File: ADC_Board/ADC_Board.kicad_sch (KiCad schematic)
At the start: 0 parts

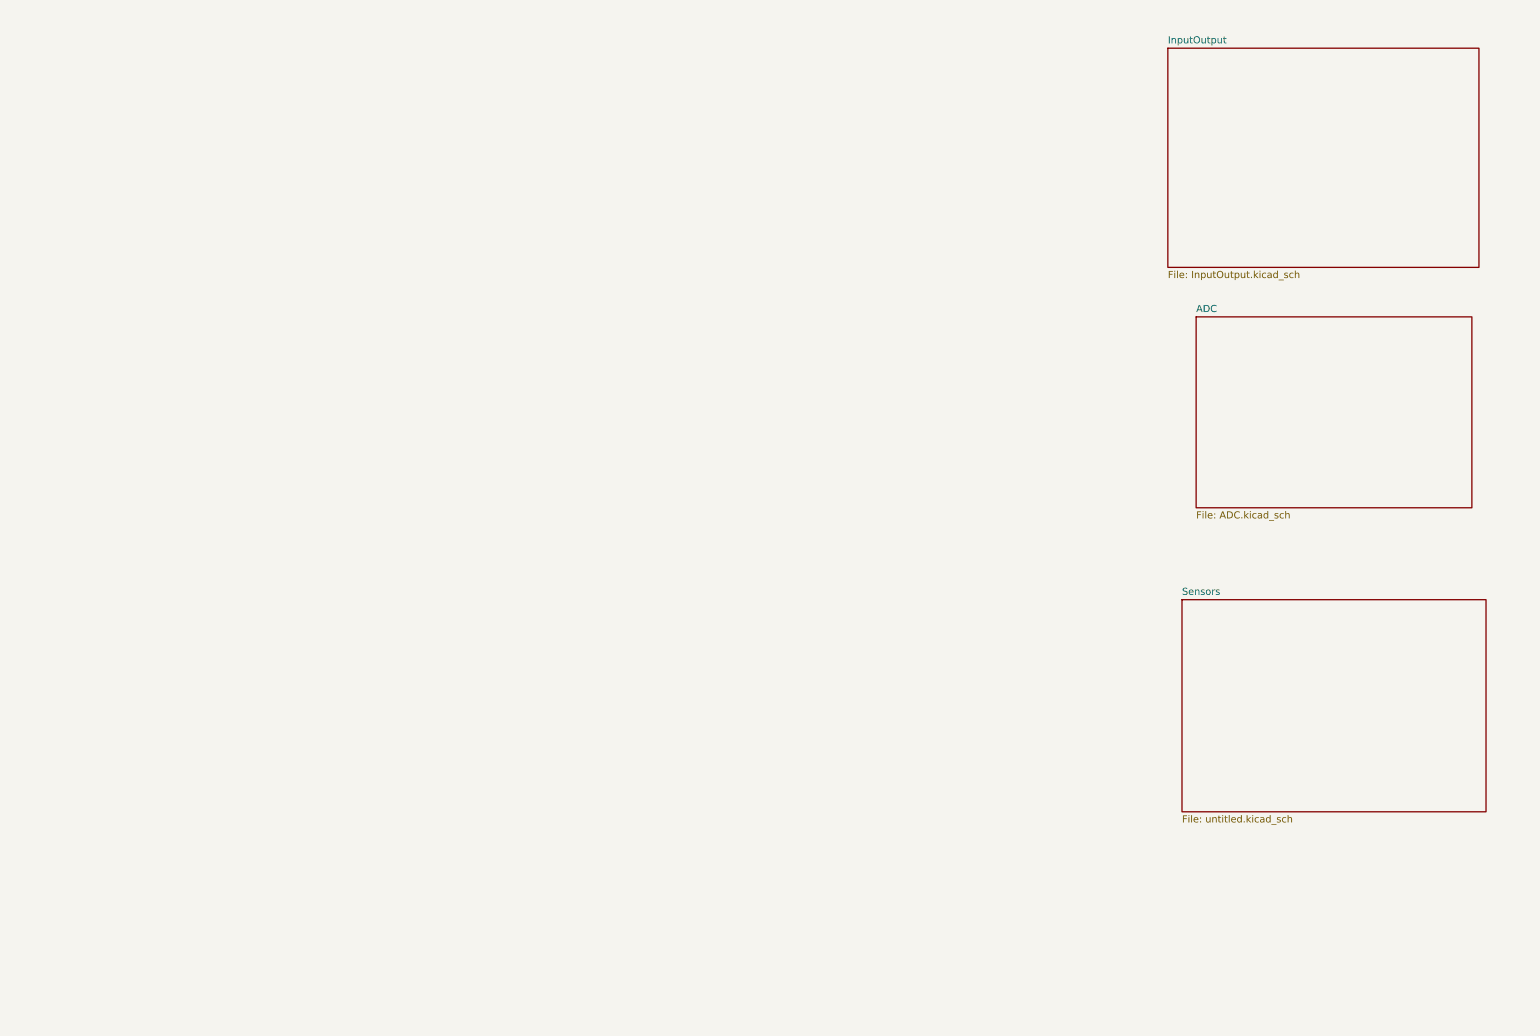
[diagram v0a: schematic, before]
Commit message: Changes made after v1 to address Lakshay and Ishaans comments
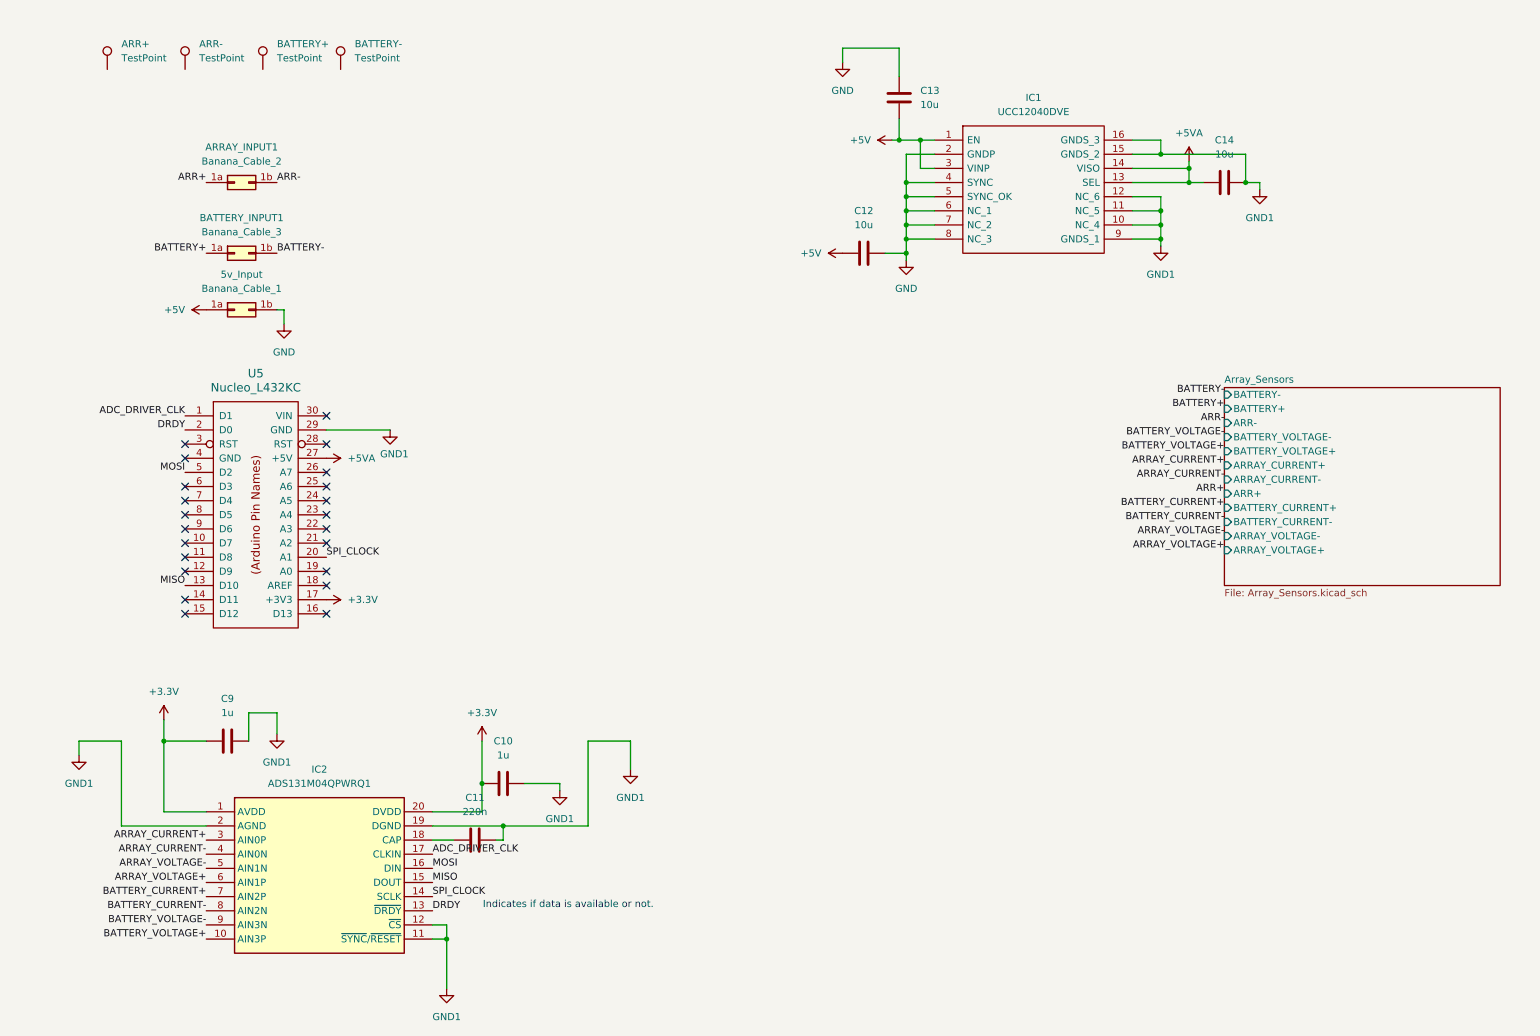
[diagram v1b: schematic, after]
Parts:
- added 5v_Input: Banana_Cable_1, symbol Connector_Generic:Conn_02x01_Row_Letter_Last
- added ARR+, ARR-, BATTERY+, BATTERY-: TestPoint, symbol Connector:TestPoint
- added ARRAY_INPUT1: Banana_Cable_2, symbol Connector_Generic:Conn_02x01_Row_Letter_Last
- added BATTERY_INPUT1: Banana_Cable_3, symbol Connector_Generic:Conn_02x01_Row_Letter_Last
- added C10, C9: 1u, symbol Device:C
- added C11: 220n, symbol Device:C
- added C12, C13, C14: 10u, symbol Device:C
- added IC1: UCC12040DVE, SOIC127P1030X265-16N, symbol UCC12040DVE:UCC12040DVE
- added IC2: ADS131M04QPWRQ1, SOP65P640X120-20N, symbol ADS131M04QPWRQ1:ADS131M04QPWRQ1
- added U5: Nucleo_L432KC, symbol utsvt-microcontrollers:Nucleo_L432KC
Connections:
- new net: C11.2, IC2.18 (CAP)
- new net +3.3V: C10.1, C9.1, IC2.1 (AVDD), IC2.20 (DVDD), U5.17 (+3V3)
- new net +5V: 5v_Input.1a (Pin_1a), C12.1, C13.2, IC1.1 (EN), IC1.3 (VINP)
- new net +5VA: C14.1, IC1.13 (SEL), IC1.14 (VISO), U5.27 (+5V)
- new net ADC_DRIVER_CLK: IC2.17 (CLKIN), U5.1 (D1)
- new net ARR+: ARRAY_INPUT1.1a (Pin_1a)
- new net ARR-: ARRAY_INPUT1.1b (Pin_1b)
- new net ARRAY_CURRENT+: IC2.3 (AIN0P)
- new net ARRAY_CURRENT-: IC2.4 (AIN0N)
- new net ARRAY_VOLTAGE+: IC2.6 (AIN1P)
- new net ARRAY_VOLTAGE-: IC2.5 (AIN1N)
- new net BATTERY+: BATTERY_INPUT1.1a (Pin_1a)
- new net BATTERY-: BATTERY_INPUT1.1b (Pin_1b)
- new net BATTERY_CURRENT+: IC2.7 (AIN2P)
- new net BATTERY_CURRENT-: IC2.8 (AIN2N)
- new net BATTERY_VOLTAGE+: IC2.10 (AIN3P)
- new net BATTERY_VOLTAGE-: IC2.9 (AIN3N)
- new net DRDY: IC2.13 (~{DRDY}), U5.2 (D0)
- new net GND: 5v_Input.1b (Pin_1b), C12.2, C13.1, IC1.2 (GNDP), IC1.4 (SYNC), IC1.5 (SYNC_OK), IC1.6 (NC_1), IC1.7 (NC_2), IC1.8 (NC_3)
- new net GND1: C10.2, C11.1, C14.2, C9.2, IC1.10 (NC_4), IC1.11 (NC_5), IC1.12 (NC_6), IC1.15 (GNDS_2), IC1.16 (GNDS_3), IC1.9 (GNDS_1), IC2.11 (~{SYNC}/~{RESET}), IC2.12 (~{CS}), IC2.19 (DGND), IC2.2 (AGND), U5.29 (GND)
- new net MISO: IC2.15 (DOUT), U5.13 (D10)
- new net MOSI: IC2.16 (DIN), U5.5 (D2)
- new net SPI_CLOCK: IC2.14 (SCLK), U5.20 (A1)
- no-connect marks 0 -> 22
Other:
- removed sheet ADC
- removed sheet InputOutput
- removed sheet Sensors
- added sheet Array_Sensors (Array_Sensors.kicad_sch)
- note added: "Indicates if data is available or not."

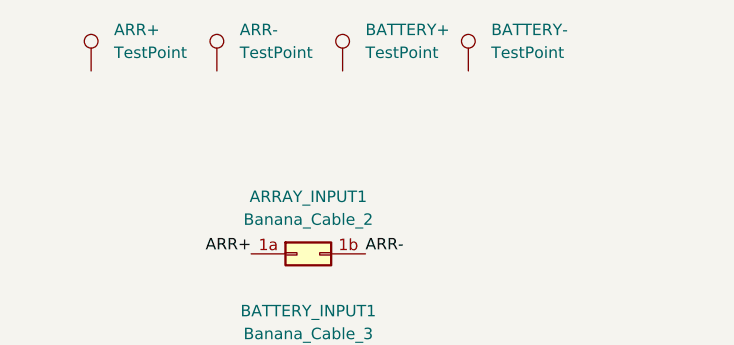
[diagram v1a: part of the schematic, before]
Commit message: Added RC filters to first commit of v2 during workday
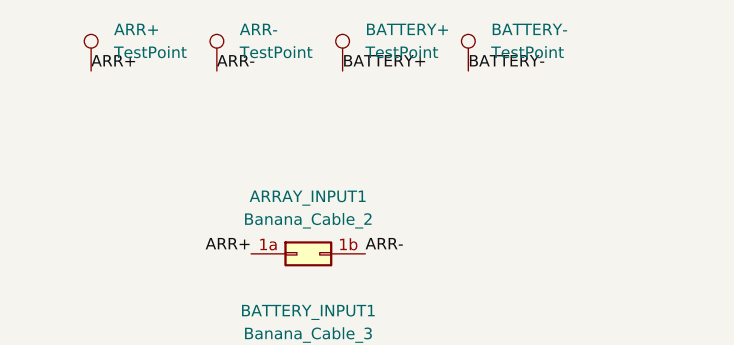
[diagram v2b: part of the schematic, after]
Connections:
- net ARR+: now also ARR+.1
- net ARR-: now also ARR-.1
- net BATTERY+: now also BATTERY+.1
- net BATTERY-: now also BATTERY-.1
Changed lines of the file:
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@@
+		)
+	)
+	(label "BATTERY+"
+		(at 55.88 22.86 0)
+		(fields_autoplaced yes)
+		(effects
+			(font
+				(size 1.27 1.27)
+			)
+			(justify left bottom)
 		)
 	)
@@
 		)
 	)
+	(label "ARR+"
+		(at 27.94 22.86 0)
+		(fields_autoplaced yes)
+		(effects
+			(font
+				(size 1.27 1.27)
+			)
+			(justify left bottom)
+		)
+	)
 	(label "ARRAY_CURRENT-"
 		(at 228.6 96.52 180)
@@
 		)
 	)
+	(label "ARR-"
+		(at 41.91 22.86 0)
+		(fields_autoplaced yes)
+		(effects
+			(font
+				(size 1.27 1.27)
+			)
+			(justify left bottom)
+		)
+	)
 	(label "SPI_CLOCK"
 		(at 67.31 110.49 0)
@@
 		)
 	)
+	(label "BATTERY-"
+		(at 69.85 22.86 0)
+		(fields_autoplaced yes)
+		(effects
+			(font
+				(size 1.27 1.27)
+			)
+			(justify left bottom)
+		)
+	)

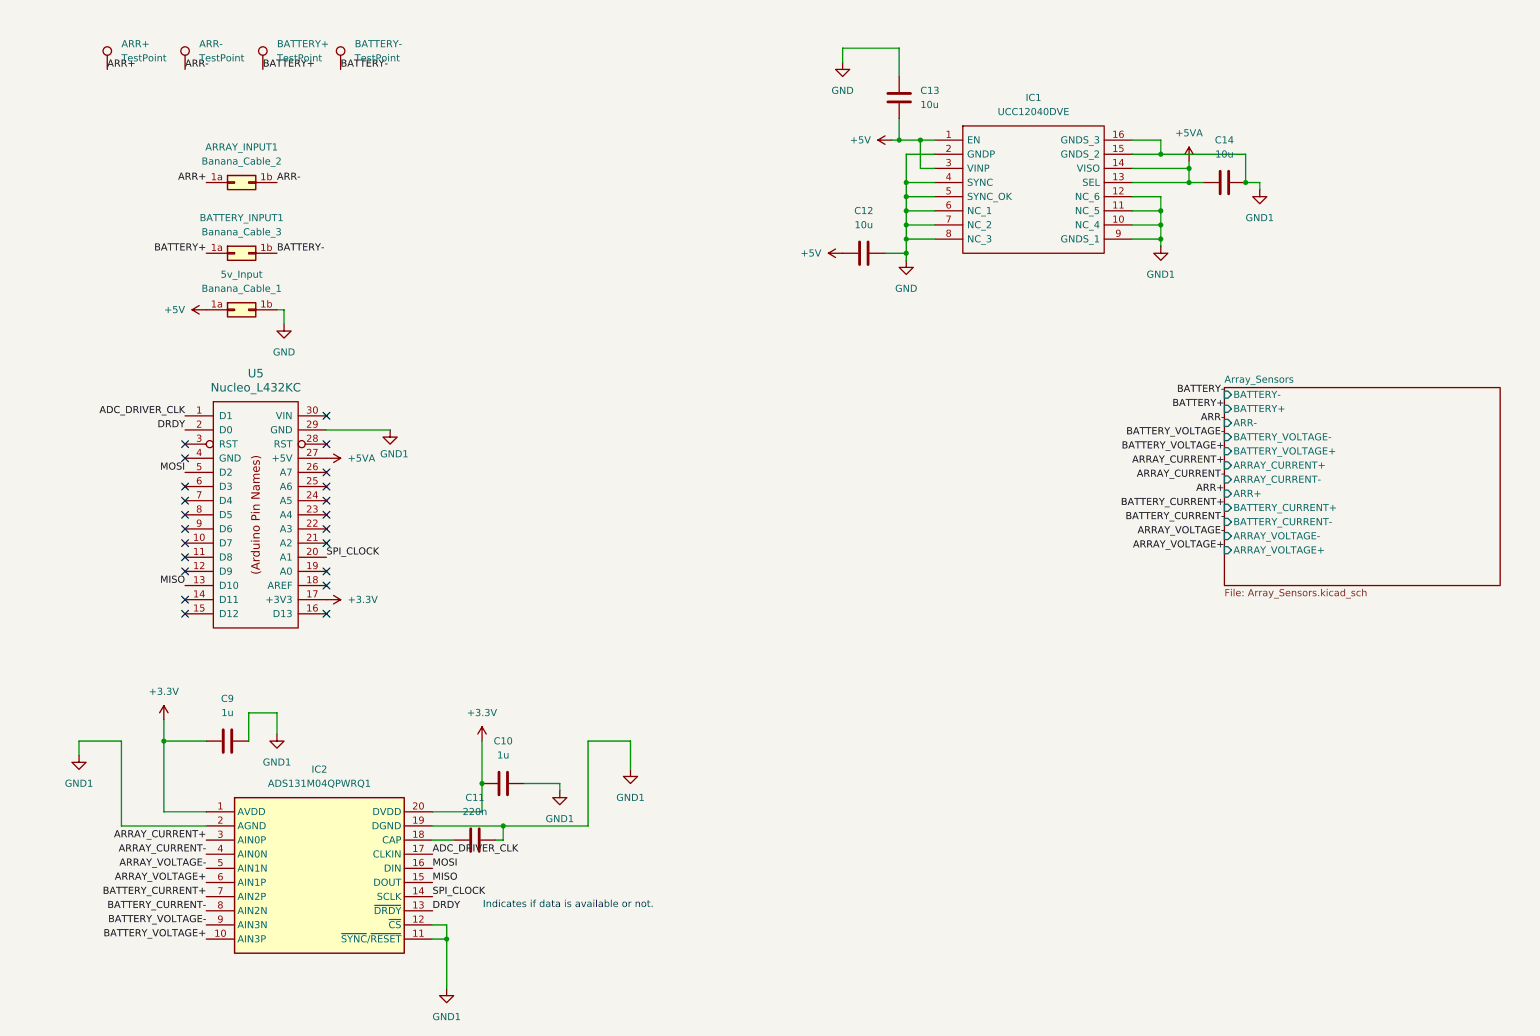
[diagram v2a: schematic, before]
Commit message: Addressed the comments from Champeys review. Including adding an isolation chip for the SPI. Changing Amplifiers to non-isolating to avoid running signal through ADC twice. As well as a few small changes to pin connections in ADC and DC-DC isolator.
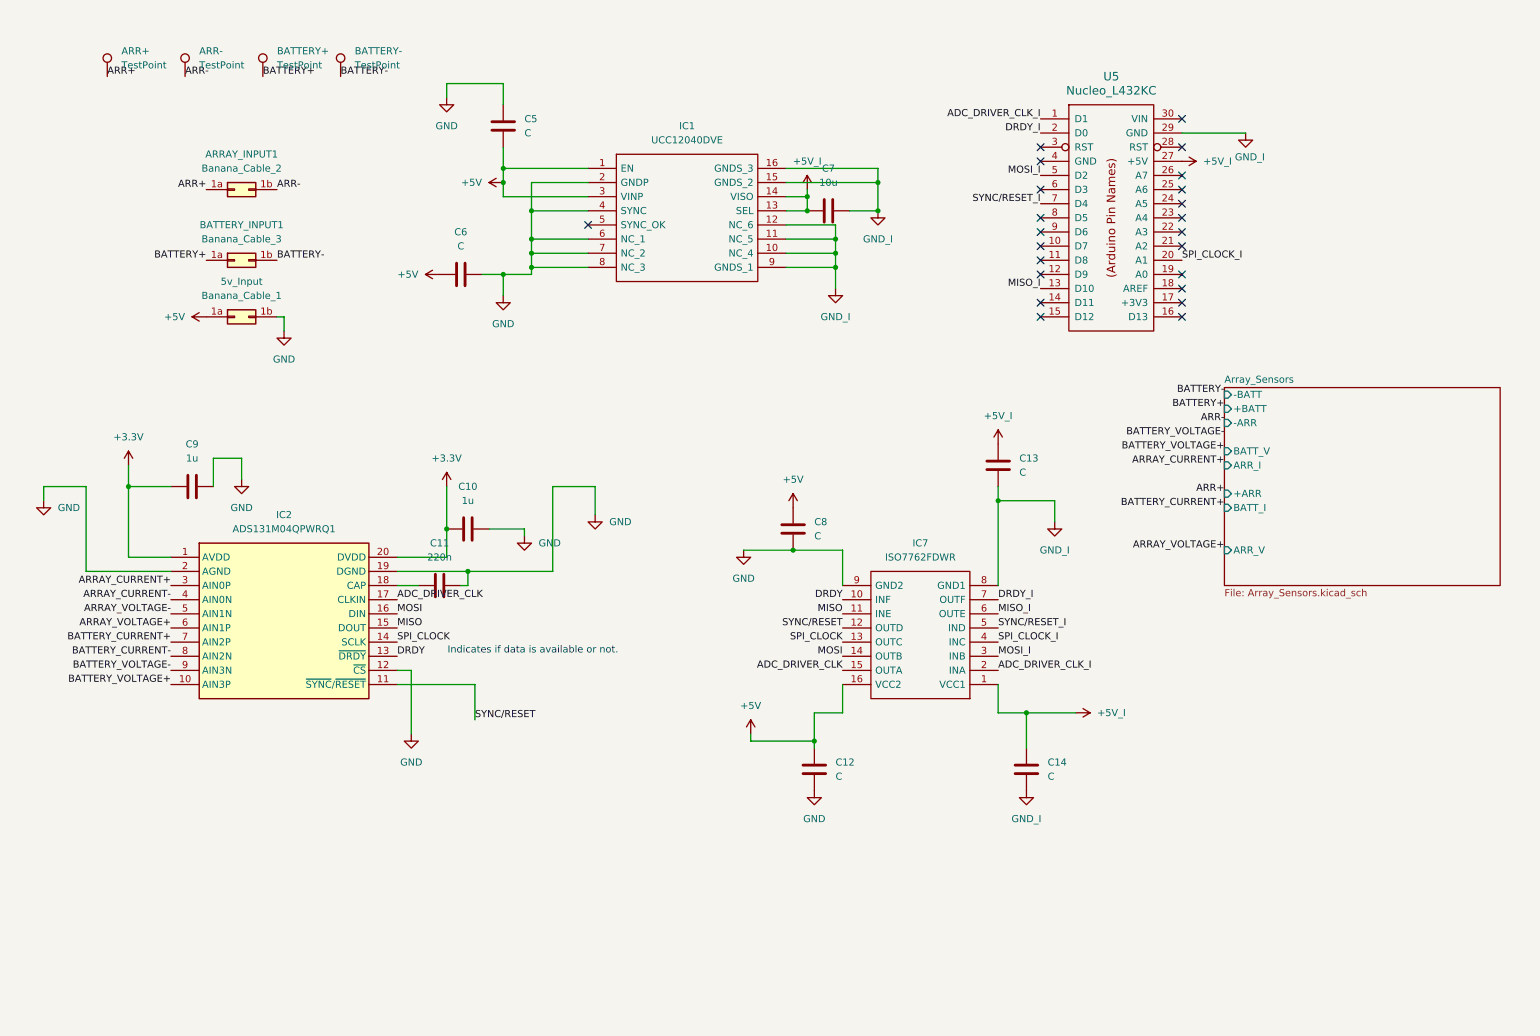
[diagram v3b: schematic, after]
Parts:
- added C5, C6, C8: C, symbol Device:C
- added C7: 10u, symbol Device:C
- added IC7: ISO7762FDWR, SOIC127P1030X265-16N, symbol ISO7762FDWR:ISO7762FDWR
- C12, C13, C14: value 10u -> C
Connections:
- net +3.3V: no longer U5.17 (+3V3)
- net +5V: now also C5.2, C6.1, C8.1, IC7.16 (VCC2); no longer C13.2
- net ADC_DRIVER_CLK: now also IC7.15 (OUTA); no longer U5.1 (D1)
- net DRDY: now also IC7.10 (INF); no longer U5.2 (D0)
- net GND: now also C10.2, C11.1, C9.2, IC2.12 (~{CS}), IC2.19 (DGND), IC2.2 (AGND), C5.1, C6.2, C8.2, IC7.9 (GND2); no longer C13.1, IC1.5 (SYNC_OK)
- net MISO: now also IC7.11 (INE); no longer U5.13 (D10)
- net MOSI: now also IC7.14 (OUTB); no longer U5.5 (D2)
- net SPI_CLOCK: now also IC7.13 (OUTC); no longer U5.20 (A1)
- net SYNC/RESET_I: now reaches U5.7 (D4)
- net SYNC/RESET_I: now also IC7.5 (IND)
- net +5VA renamed +5V_I
- net +5V_I: now also C13.1, C7.1, IC7.1 (VCC1)
- net GND1 renamed GND_I
- net GND_I: now also C13.2, C7.2, IC7.8 (GND1); no longer C10.2, C11.1, C9.2, IC2.11 (~{SYNC}/~{RESET}), IC2.12 (~{CS}), IC2.19 (DGND), IC2.2 (AGND)
- new net ADC_DRIVER_CLK_I: IC7.2 (INA), U5.1 (D1)
- new net DRDY_I: IC7.7 (OUTF), U5.2 (D0)
- new net MISO_I: IC7.6 (OUTE), U5.13 (D10)
- new net MOSI_I: IC7.3 (INB), U5.5 (D2)
- new net SPI_CLOCK_I: IC7.4 (INC), U5.20 (A1)
- new net SYNC/RESET: IC2.11 (~{SYNC}/~{RESET}), IC7.12 (OUTD)
- no-connect marks 22 -> 23
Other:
- sheet Array_Sensors ports: added +ARR, +BATT, -ARR, -BATT, ARR_I, ARR_V, BATT_I, BATT_V; removed ARR+, ARR-, ARRAY_CURRENT+, ARRAY_CURRENT-, ARRAY_VOLTAGE+, ARRAY_VOLTAGE-, BATTERY+, BATTERY-, BATTERY_CURRENT+, BATTERY_CURRENT-, BATTERY_VOLTAGE+, BATTERY_VOLTAGE-
- moved on the sheet: 5v_Input, ARR+, ARR-, ARRAY_INPUT1, BATTERY+, BATTERY-, BATTERY_INPUT1, C10, C11, C9, IC2, U5
